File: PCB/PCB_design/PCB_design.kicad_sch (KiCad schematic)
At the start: 7 parts, among them J1 Conn_01x02_Pin, U1 NE555D

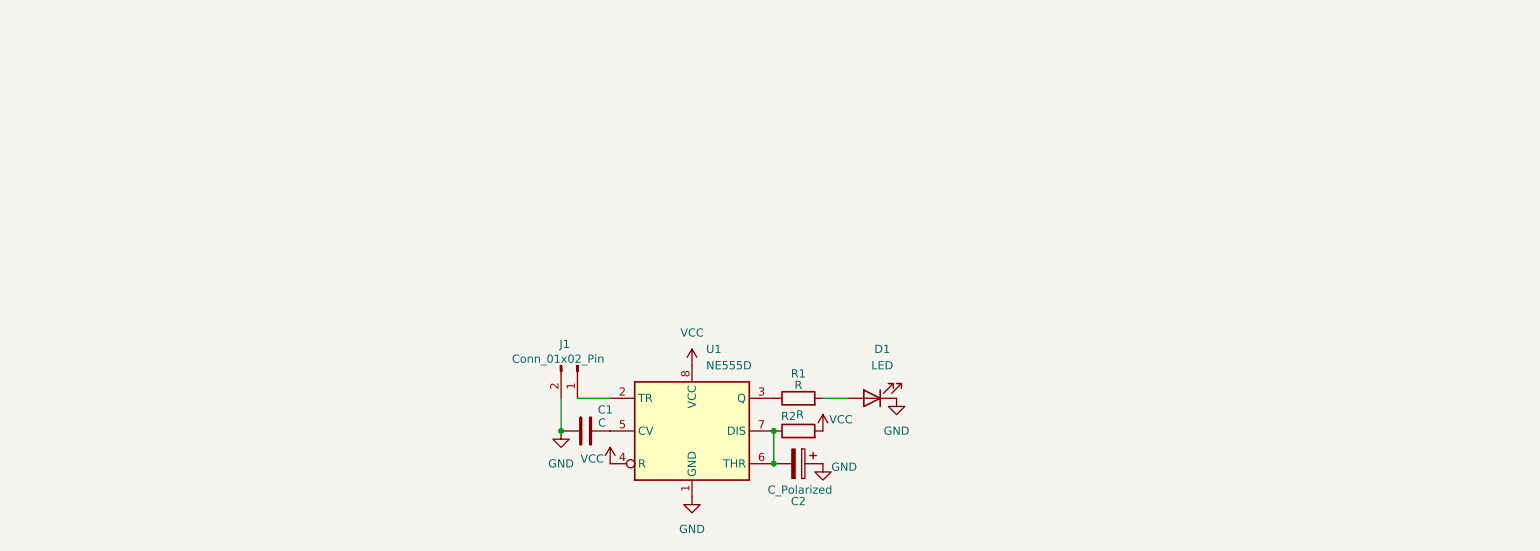
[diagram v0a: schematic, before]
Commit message: Début bloc AC et Flyback/LDO
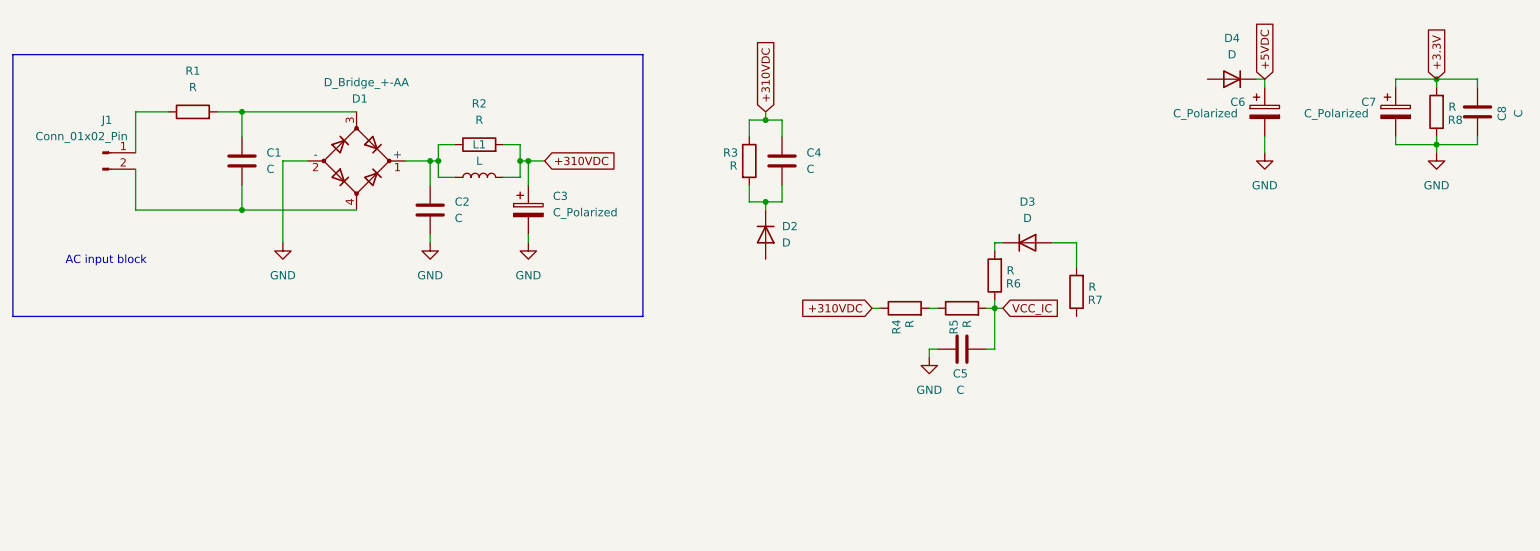
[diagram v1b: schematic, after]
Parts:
- removed C2: C_Polarized, Capacitor_SMD:C_0603_1608Metric, symbol Device:C_Polarized
- removed D1: LED, LED_SMD:LED_0603_1608Metric, symbol Device:LED
- removed U1: NE555D, Package_SO:SOIC-8_3.9x4.9mm_P1.27mm, symbol Timer:NE555D
- added C2, C4, C5, C8: C, symbol Device:C
- added C3, C6, C7: C_Polarized, symbol Device:C_Polarized
- added D1: D_Bridge_+-AA, symbol Device:D_Bridge_+-AA
- added D2, D3, D4: D, symbol Device:D
- added L1: L, symbol Device:L
- added R3, R4, R5, R6, R7, R8: R, symbol Device:R
- C1: footprint Capacitor_SMD:C_0603_1608Metric -> (none)
- J1: footprint Connector_PinHeader_2.54mm:PinHeader_1x02_P2.54mm_Vertical -> (none)
- R1, R2: footprint Resistor_SMD:R_0603_1608Metric -> (none)
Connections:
- net GND: now also C2.2, C3.2, C5.1, C6.2, C7.2, C8.1, D1.2 (-), R8.1; no longer C1.1, J1.2 (Pin_2)
- net at R1.2: now also C1.1, D1.3
- net at R2.1: now also C2.1, D1.1 (+), L1.1
- net at J1.1 (Pin_1): now also R1.1
- net at C1.2: now also J1.2 (Pin_2), D1.4
- net VCC renamed +310VDC
- net +310VDC: now also C3.1, C4.1, L1.2, R3.1, R4.1
- new net: C4.2, D2.1 (K), R3.2
- new net: R4.2, R5.1
- new net: D3.1 (K), R6.2
- new net: D3.2 (A), R7.2
- new net +3.3V: C7.1, C8.2, R8.2
- new net +5VDC: C6.1, D4.1 (K)
- new net VCC_IC: C5.2, R5.2, R6.1
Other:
- note added: "AC input block"

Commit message: Début schematic
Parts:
- removed C5: C, symbol Device:C
- removed J1: Conn_01x02_Pin, symbol Connector:Conn_01x02_Pin
- removed L1: L, symbol Device:L
- removed R1: R, symbol Device:R
- added C5: 4,7u, symbol Device:C_Polarized
- added F1: 68, symbol Device:Fuse
- added J2: Conn_01x03_Pin, symbol Connector:Conn_01x03_Pin
- added L2: 3m, symbol Device:L_Ferrite
- added R10: 3,9k, symbol Device:R
- added R11: 2M, symbol Device:R
- added R9: 430k, symbol Device:R
- added T1: Transformer_1P_2S, symbol Device:Transformer_1P_2S
- added U1: SCJT1117B-3.3-A, Package_TO_SOT_SMD:SOT-223-3_TabPin2, symbol Regulator_Linear:AMS1117-3.3
- added U2: ~, symbol Touch_Switch_Custom:S7133S
- C1: value C -> 0,1u
- C3: value C_Polarized -> 2,2u
- C4: value C -> 100p
- C6: value C_Polarized -> 470u
- C7: value C_Polarized -> 330u
- R2: value R -> 5,6k
- R3: value R -> 430k
- R5: value R -> 1,5
- R6: value R -> 2M
- R7: value R -> 24k
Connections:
- net +3.3V: now also U1.2 (VO)
- net +310VDC: now also R6.1, L2.2, R9.1, T1.1 (AA); no longer R4.1
- net +5VDC: now also U1.3 (VI)
- net GND: now also R5.1, C5.2, R10.1, T1.6 (SD), U2.7 (GND); no longer C6.2, C7.2, C8.1, R8.1
- net VCC_IC: now also R4.1, C5.1, R11.2, U2.1 (VCC); no longer R5.2, R6.1
- net at C1.2, D1.4: now also J2.2 (Pin_2), J2.3 (Pin_3)
- net at C2.1, D1.1 (+), R2.1: now also L2.1
- net at C4.2, D2.1 (K), R3.2: now also R9.2
- net at R4.2: now also D3.1 (K); no longer R5.1
- net at C1.1, D1.3: now also F1.2
- net C: now reaches D2.2 (A)
- net C: now also T1.2 (AB), U2.5 (C), U2.6 (C)
- net at D4.2 (A): now also T1.3 (SA)
- net at R6.2: now also R11.1; no longer D3.1 (K)
- net at R7.2: now also R10.2, U2.2 (FB); no longer D3.2 (A)
- net Vaux: now reaches R7.1
- net Vaux: now also D3.2 (A), T1.5 (SC)
- new net: F1.1, J2.1 (Pin_1)
- new net: R5.2, U2.4 (CS)
- new net GND2: C6.2, C7.2, C8.1, R8.1, T1.4 (SB), U1.1 (GND)
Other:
- note added: "AC input"
- note added: "Driver"
- note added: "Snubber"
- note added: "Transformer & LDO"
- note removed: "AC input block"
- moved on the sheet: C4, C6, C7, C8, D2, D4, R3, R7, R8

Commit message: Assignation footprints
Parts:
- removed C5: 4,7u, symbol Device:C_Polarized
- added C9: 4,7u, Capacitor_SMD:C_0805_2012Metric, symbol Device:C
- added D5, D6, D7, D8: D, Diode_SMD:D_SOD-123, symbol Device:D
- added J3, J4, J5, J6: Conn_01x01_Pin, symbol Connector:Conn_01x01_Pin
- added J7: Conn_02x04_Counter_Clockwise, Connector_PinHeader_2.54mm:PinHeader_2x04_P2.54mm_Vertical, symbol Connector_Generic:Conn_02x04_Counter_Clockwise
- added K1, K2, K3, K4: Relay_SPST-NO, Touch_Switch_Custom:FH17-1A2STLE-DC5V, symbol Relay:Relay_SPST-NO
- added Q1, Q2, Q3, Q4: MMBT3904, Package_TO_SOT_SMD:SOT-23, symbol Transistor_BJT:MMBT3904
- added R1, R12, R13, R14: 10k, Resistor_SMD:R_0603_1608Metric, symbol Device:R
- added R15: 100, symbol Device:R
- C8: value C -> 0,1u
- D1: footprint (none) -> Diode_SMD:Diode_Bridge_Diotec_ABS
- D2, D3, D4: footprint (none) -> Diode_SMD:D_SMA
- F1: footprint (none) -> Touch_Switch_Custom:Fuse
- L2: footprint (none) -> Inductor_THT:L_Radial_D7.5mm_P3.50mm_Fastron_07P
- R10, R11, R5, R6, R7: footprint (none) -> Resistor_SMD:R_1206_3216Metric
- R4: value R -> 100
- R8: value R -> 1k; footprint (none) -> Resistor_SMD:R_0805_2012Metric
- U2: footprint (none) -> Package_SO:SOP-8_3.9x4.9mm_P1.27mm
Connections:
- net +3.3V: now also J7.8 (Pin_8)
- net +5VDC: now also D5.1 (K), D6.1 (K), D7.1 (K), D8.1 (K), K1.A1, K2.A1, K3.A1, K4.A1
- net GND: now also C9.2
- net GND2: now also J7.7 (Pin_7), Q1.2 (E), Q2.2 (E), Q3.2 (E), Q4.2 (E), R1.1, R12.1, R13.1, R14.1
- net VCC_IC: now also C9.1
- net L: now reaches F1.1, J2.1 (Pin_1)
- net L: now also K1.13, K2.13, K3.13, K4.13
- net N: now reaches C1.2, D1.4, J2.2 (Pin_2), J2.3 (Pin_3)
- net at C4.2, R3.2, R9.2: now also R15.1; no longer D2.1 (K)
- new net: D5.2 (A), K1.A2, Q1.3 (C)
- new net: J3.1 (Pin_1), K1.14
- new net: D6.2 (A), K2.A2, Q2.3 (C)
- new net: D7.2 (A), K3.A2, Q3.3 (C)
- new net: J6.1 (Pin_1), K4.14
- new net: D8.2 (A), K4.A2, Q4.3 (C)
- new net: D2.1 (K), R15.2
- new net: J4.1 (Pin_1), K2.14
- new net: J5.1 (Pin_1), K3.14
- new net CT1: J7.5 (Pin_5), Q1.1 (B), R1.2
- new net CT2: J7.4 (Pin_4), Q2.1 (B), R12.2
- new net CT3: J7.3 (Pin_3), Q3.1 (B), R13.2
- new net CT4: J7.2 (Pin_2), Q4.1 (B), R14.2
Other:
- note added: "Driver-touch connector"
- note added: "May-July 2024"
- note added: "Relay 1"
- note added: "Relay 2"
- note added: "Relay 3"
- note added: "Relay 4"
- note added: "Space for more Cs"
- note added: "Touch switch prototype"
- moved on the sheet: C1, C2, C3, C4, C6, C7, C8, D1, D2, D3, D4, F1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

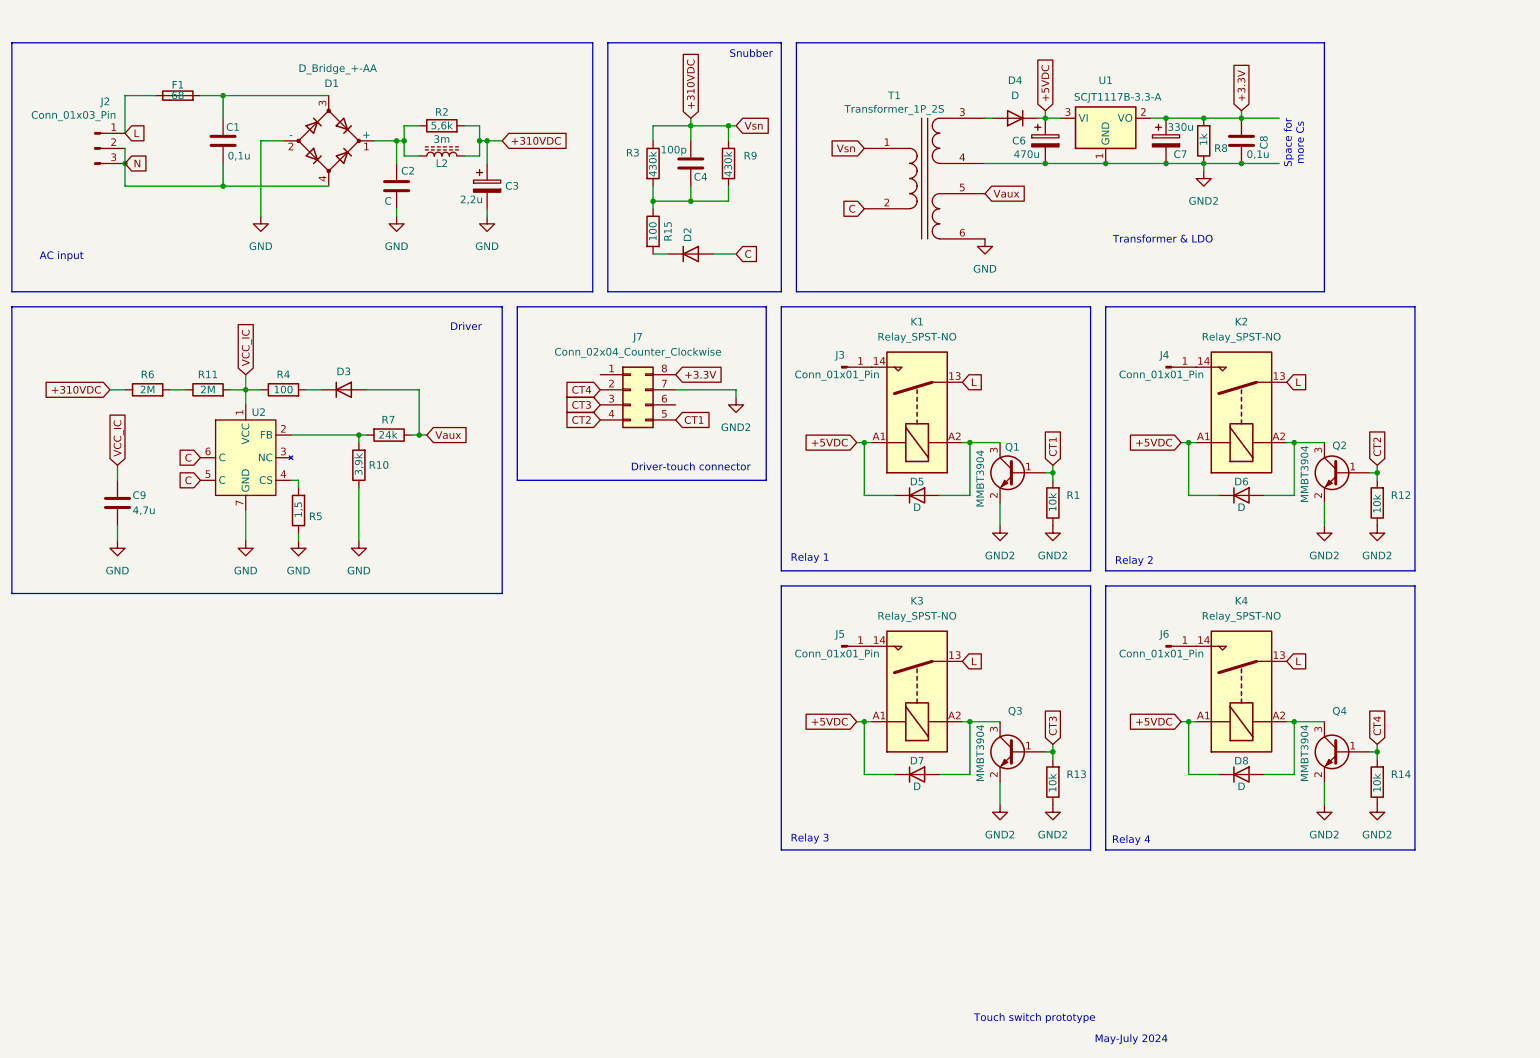
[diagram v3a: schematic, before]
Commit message: Début routage
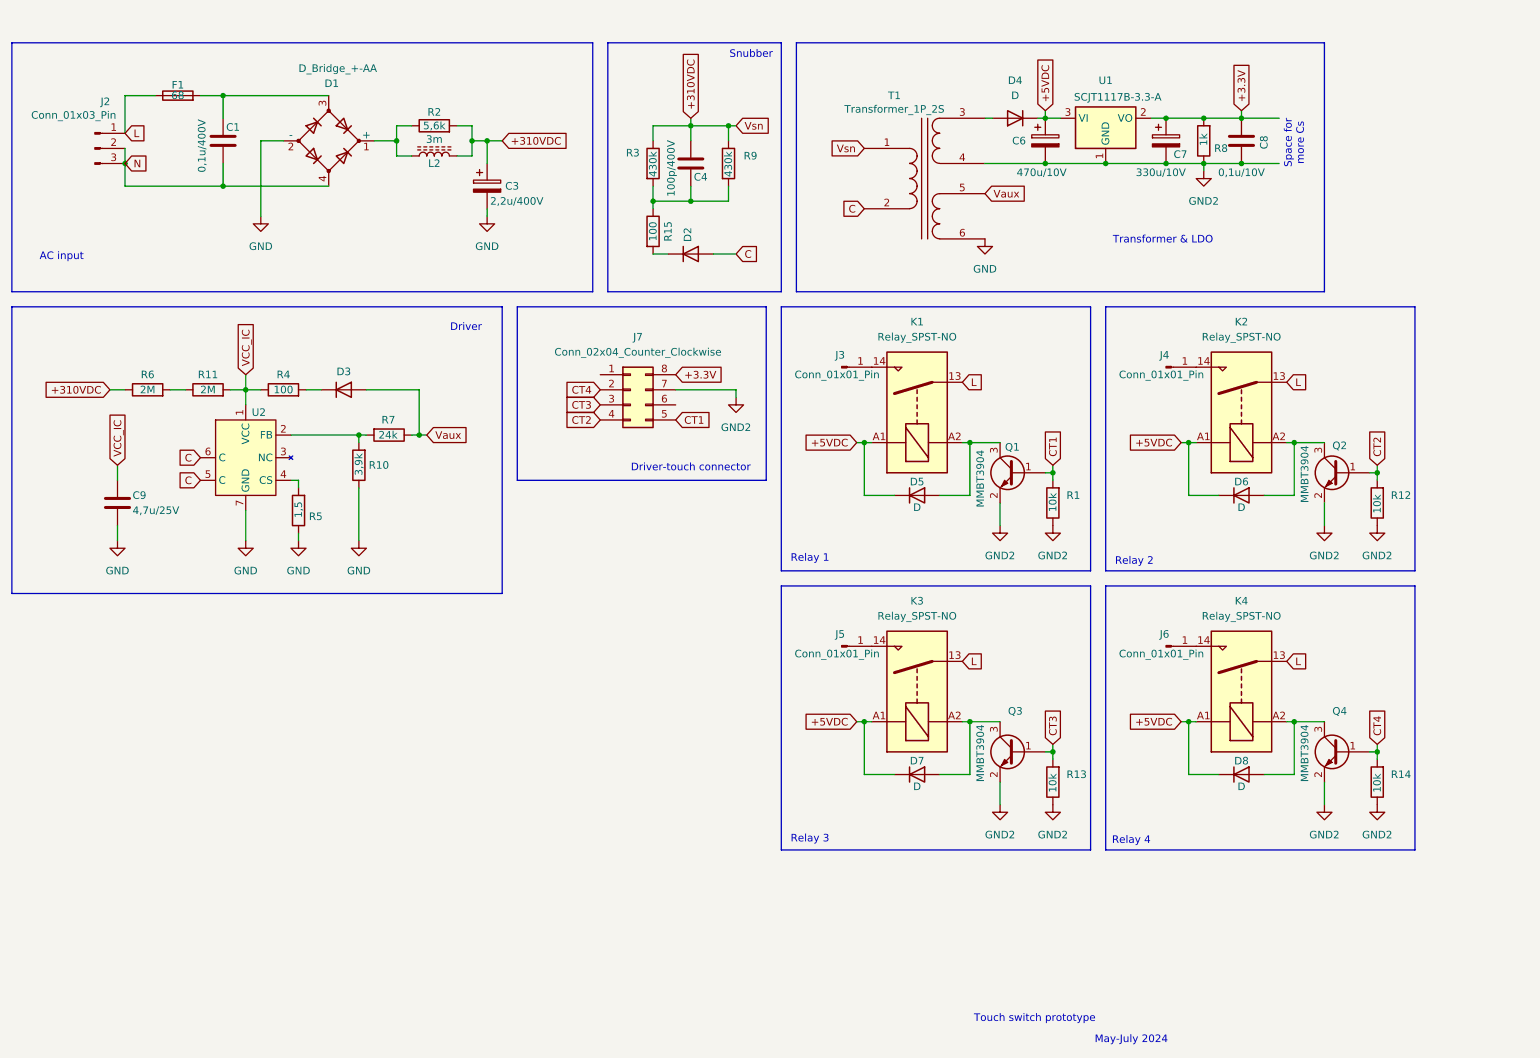
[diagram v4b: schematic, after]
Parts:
- removed C2: C, symbol Device:C
- C1: value 0,1u -> 0,1u/400V; footprint (none) -> Touch_Switch_Custom:MKP-X2-100NR10
- C3: value 2,2u -> 2,2u/400V
- C4: value 100p -> 100p/400V; footprint (none) -> Capacitor_SMD:C_0805_2012Metric
- C6: value 470u -> 470u/10V
- C7: value 330u -> 330u/10V
- C8: value 0,1u -> 0,1u/10V; footprint (none) -> Capacitor_SMD:C_0805_2012Metric
- C9: value 4,7u -> 4,7u/25V
- R1, R12, R13, R14: footprint Resistor_SMD:R_0603_1608Metric -> Resistor_SMD:R_0805_2012Metric
- R15, R2, R3, R9: footprint (none) -> Resistor_SMD:R_1206_3216Metric
- R4: footprint (none) -> Resistor_SMD:R_0805_2012Metric
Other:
- moved on the sheet: L2, R2

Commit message: Routage : regroupement des blocs
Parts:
- C3, C6, C7: footprint (none) -> Capacitor_THT:CP_Radial_D8.0mm_P3.50mm
- J2: footprint (none) -> Connector_PinHeader_2.54mm:PinHeader_1x03_P2.54mm_Vertical
- J3, J4, J5, J6: footprint (none) -> Connector_PinHeader_2.54mm:PinHeader_1x01_P2.54mm_Vertical
- T1: footprint (none) -> Touch_Switch_Custom:Transformer_V2
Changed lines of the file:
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@@
 			)
 		)
-		(property "Footprint" ""
+		(property "Footprint" "Touch_Switch_Custom:Transformer_V2"
 			(at 179.07 48.26 0)
 			(effects
@@
 			)
 		)
-		(property "Footprint" ""
+		(property "Footprint" "Connector_PinHeader_2.54mm:PinHeader_1x03_P2.54mm_Vertical"
 			(at 39.37 43.18 0)
 			(effects
@@
 			)
 		)
-		(property "Footprint" ""
+		(property "Footprint" "Capacitor_THT:CP_Radial_D8.0mm_P3.50mm"
 			(at 200.3552 45.72 0)
 			(effects
@@
 			)
 		)
-		(property "Footprint" ""
+		(property "Footprint" "Capacitor_THT:CP_Radial_D8.0mm_P3.50mm"
 			(at 220.6752 45.72 0)
 			(effects
@@
 			)
 		)
-		(property "Footprint" ""
+		(property "Footprint" "Connector_PinHeader_2.54mm:PinHeader_1x01_P2.54mm_Vertical"
 			(at 219.71 127 0)
 			(effects
@@
 			)
 		)
-		(property "Footprint" ""
+		(property "Footprint" "Capacitor_THT:CP_Radial_D8.0mm_P3.50mm"
 			(at 106.3752 53.34 0)
 			(effects
@@
 			)
 		)
-		(property "Footprint" ""
+		(property "Footprint" "Connector_PinHeader_2.54mm:PinHeader_1x01_P2.54mm_Vertical"
 			(at 165.1 80.01 0)
 			(effects
@@
 			)
 		)
-		(property "Footprint" ""
+		(property "Footprint" "Connector_PinHeader_2.54mm:PinHeader_1x01_P2.54mm_Vertical"
 			(at 219.71 80.01 0)
 			(effects
@@
 			)
 		)
-		(property "Footprint" ""
+		(property "Footprint" "Connector_PinHeader_2.54mm:PinHeader_1x01_P2.54mm_Vertical"
 			(at 165.1 127 0)
 			(effects

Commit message: Routage compact
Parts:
- removed U2: ~, Package_SO:SOP-8_3.9x4.9mm_P1.27mm, symbol Touch_Switch_Custom:S7133S
- added U3: ~, Package_SO:SOP-8_3.9x4.9mm_P1.27mm, symbol Touch_Switch_Custom:S7133S
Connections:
- net C: now also U3.5 (C), U3.6 (C)
- net GND: now also U3.8 (GND)
- net VCC_IC: now also U3.1 (VCC)
- net at R10.2, R7.2: now also U3.2 (FB)
- net at R5.2: now also U3.4 (CS)
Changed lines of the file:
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@@
-	)
-	(symbol
-		(lib_id "Touch_Switch_Custom:S7133S")
-		(at 64.77 87.63 0)
-		(unit 1)
-		(exclude_from_sim no)
-		(in_bom yes)
-		(on_board yes)
-		(dnp no)
-		(property "Reference" "U2"
-			(at 65.786 87.63 0)
-			(effects
-				(font
-					(size 1.27 1.27)
-				)
-				(justify left)
-			)
-		)
-		(property "Value" "~"
-			(at 66.9641 87.63 0)
-			(effects
-				(font
-					(size 1.27 1.27)
-				)
-				(justify left)
-			)
-		)
-		(property "Footprint" "Package_SO:SOP-8_3.9x4.9mm_P1.27mm"
-			(at 64.77 87.63 0)
-			(effects
-				(font
-					(size 1.27 1.27)
-				)
-				(hide yes)
-			)
-		)
-		(property "Datasheet" ""
-			(at 64.77 87.63 0)
-			(effects
-				(font
-					(size 1.27 1.27)
-				)
-				(hide yes)
-			)
-		)
-		(property "Description" ""
-			(at 64.77 87.63 0)
-			(effects
-				(font
-					(size 1.27 1.27)
-				)
-				(hide yes)
-			)
-		)
-		(pin "6"
-		)
-		(pin "1"
-		)
-		(pin "3"
-		)
-		(pin "2"
-		)
-		(pin "4"
-		)
-		(pin "7"
-		)
-		(pin "5"
-		)
-		(instances
-			(project "PCB_design"
-				(path "/6e223a1a-ee81-40df-b8c9-24ff3e142a46"
-					(reference "U2")
-					(unit 1)
-				)
-			)
-		)
 	)
 	(symbol
@@
 					(unit 1)
 				)
+			)
+		)
+	)
+	(symbol
+		(lib_name "S7133S_1")
+		(lib_id "Touch_Switch_Custom:S7133S")
+		(at 64.77 87.63 0)
+		(unit 1)
+		(exclude_from_sim no)
+		(in_bom yes)
+		(on_board yes)
+		(dnp no)
+		(property "Reference" "U3"
+			(at 65.532 87.63 0)
+			(effects
+				(font
+					(size 1.27 1.27)
+				)
+				(justify left)
+			)
+		)
+		(property "Value" "~"
+			(at 66.9641 87.63 0)
+			(effects
+				(font
+					(size 1.27 1.27)
+				)
+				(justify left)
+			)
+		)
+		(property "Footprint" "Package_SO:SOP-8_3.9x4.9mm_P1.27mm"
+			(at 64.77 87.63 0)
+			(effects
+				(font
+					(size 1.27 1.27)
+				)
+				(hide yes)
+			)
+		)
+		(property "Datasheet" ""
+			(at 64.77 87.63 0)
+			(effects
+				(font
+					(size 1.27 1.27)
+				)
+				(hide yes)
+			)
+		)
+		(property "Description" ""
+			(at 64.77 87.63 0)
+			(effects
+				(font
+					(size 1.27 1.27)
+				)
+				(hide yes)
+			)
+		)
+		(pin "7"
+		)
+		(pin "3"
+		)
+		(pin "1"
+		)
+		(pin "8"
+		)
+		(pin "4"
+		)
+		(pin "2"
+		)
+		(pin "6"
+		)
+		(pin "5"
+		)
+		(instances
+			(project "PCB_design"
+				(path "/6e223a1a-ee81-40df-b8c9-24ff3e142a46"
+					(reference "U3")
+					(unit 1)
+				)

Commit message: Ajout mounting holes
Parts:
- added H1, H2, H3, H4: MountingHole, MountingHole:MountingHole_2.2mm_M2_Pad_Via, symbol Mechanical:MountingHole
- T1: footprint Touch_Switch_Custom:Transformer_V2 -> Touch_Switch_Custom:Transformer_V2_1
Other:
- note added: "Mounting holes"
